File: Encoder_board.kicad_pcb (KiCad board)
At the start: 2 copper layers, 71 parts, among them J1 Conn_01x05_Socket_RS485, J2 CAN_OUT, J3 Conn_01x05_Socket_Encoder4, J4 Conn_01x05_Socket_Encoder1, J5 Conn_01x05_Socket_Encoder2, J6 Conn_01x05_Socket_Encoder5, J7 ST-Link_pinsocket, J8 Conn_01x05_Socket_Encoder3, SW1 SW_Boot, SW2 SW_Reset, SW3 SW_DIP_x02_CANnum, SW4 SW_User, U1 XT60_M, U2 UTRS485G-S08-R, U3 UTRS485G-S08-R, U4 MCP2562-E-P, U5 BA05CC0FP, U6 BA033CC0FP, U7 STM32G431KBTx

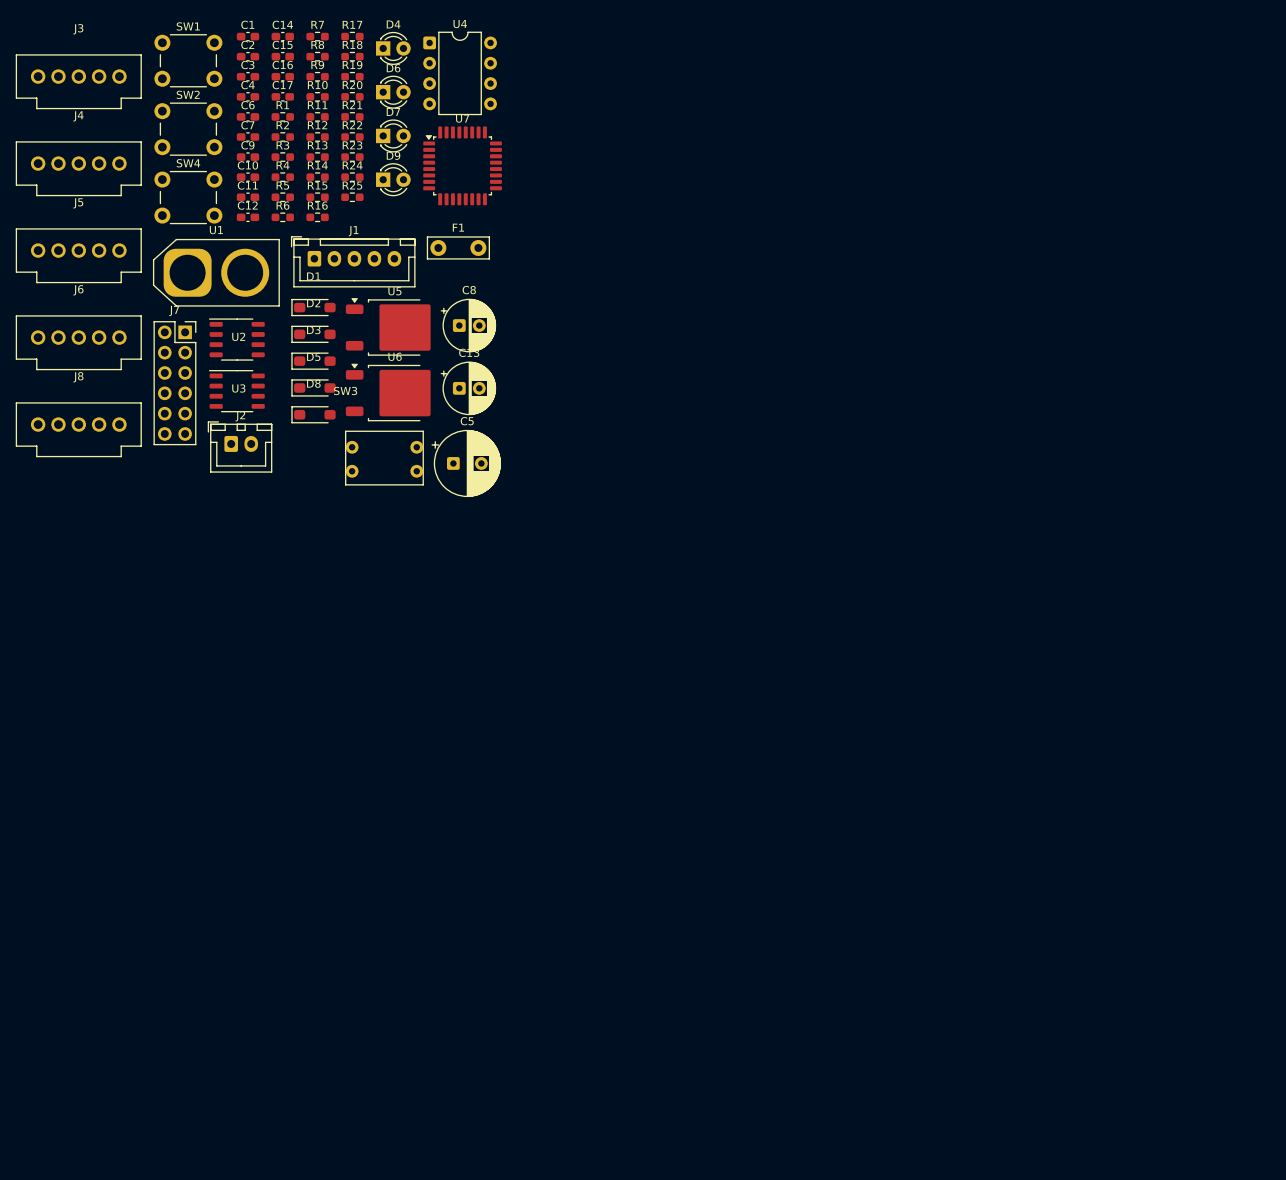
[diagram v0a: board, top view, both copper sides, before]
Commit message: 部品を配置
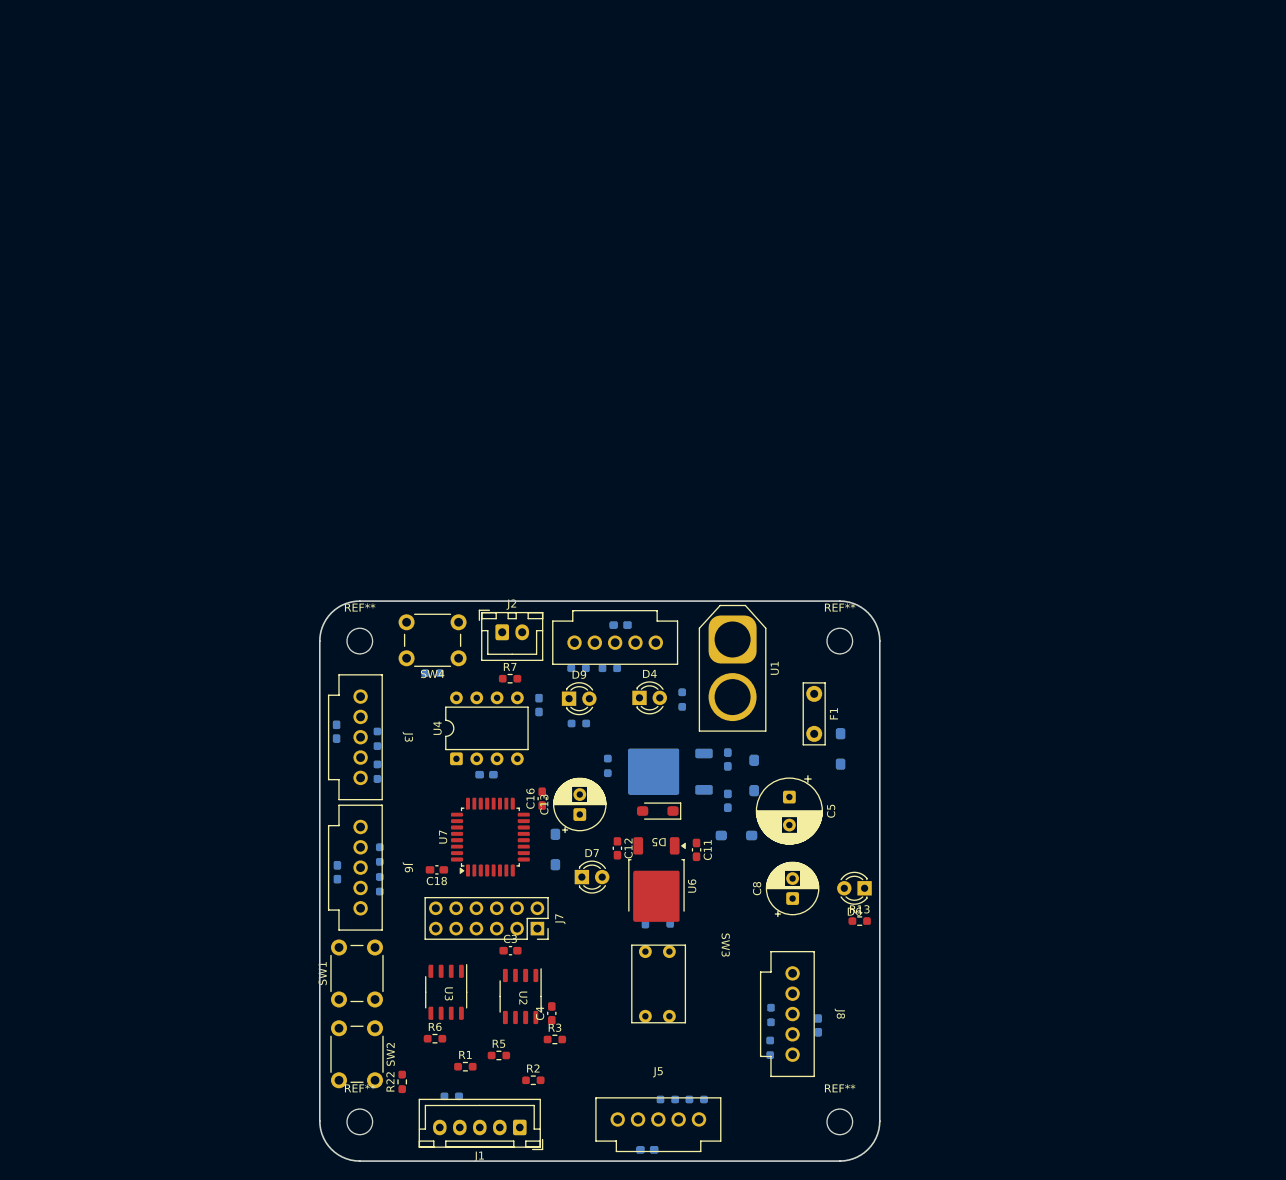
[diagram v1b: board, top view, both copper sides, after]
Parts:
- added C18: 0.1u, Capacitor_SMD:C_0603_1608Metric_Pad1.08x0.95mm_HandSolder, F.Cu at (74.7, 133.6)
- added REF**: MountingHole_3.2mm_M3, MountingHole:MountingHole_3.2mm_M3, F.Cu at (125.1, 105.0)
- added REF**: MountingHole_3.2mm_M3, MountingHole:MountingHole_3.2mm_M3, F.Cu at (65.1, 165.1)
- added REF**: MountingHole_3.2mm_M3, MountingHole:MountingHole_3.2mm_M3, F.Cu at (65.1, 105.0)
- added REF**: MountingHole_3.2mm_M3, MountingHole:MountingHole_3.2mm_M3, F.Cu at (125.1, 165.1)
- C1, C10, C14, C15, C17, C2, C6, C7, C9, D1, D2, D3, D8, R10, R11, R12, R14, R15, R16, R17, R18, R19, R20, R21, R23, R24, R25, R4, R8, R9, U5: moved to B.Cu
- moved C14 146.4 mm to (101.0, 168.6), turned to 180 degrees
- moved R17 139.7 mm to (107.2, 162.3)
- moved C17 134.0 mm to (122.4, 153.0), turned to 90 degrees
- moved J5 130.6 mm to (102.5, 159.3)
- moved R21 127.5 mm to (116.4, 155.8), turned to -90 degrees
- moved R20 126.1 mm to (116.5, 151.7), turned to 90 degrees
- moved J8 123.5 mm to (124.7, 151.7), turned to -90 degrees
- moved R2 122.0 mm to (86.8, 159.9)
- moved SW1 121.6 mm to (62.5, 149.8), turned to 90 degrees
- moved R15 121.0 mm to (103.6, 162.3), turned to 180 degrees
- moved R1 120.9 mm to (78.3, 158.2)
- moved C4 120.7 mm to (89.1, 151.5), turned to 90 degrees
- moved R22 118.3 mm to (70.4, 160.1), turned to 90 degrees
- moved SW2 117.7 mm to (67.0, 153.4), turned to -90 degrees
- moved R13 117.1 mm to (127.6, 140.0)
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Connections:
- R22 pad 1: +3V3 -> +5V
- U7 pad 10: User_LED -> CAN_num2
- U7 pad 13: CAN_num2 -> User_LED
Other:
- board outline added: 70 x 70 mm

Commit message: 配線終了。あとはシルク
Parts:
- R22: moved to B.Cu
- R4: moved to F.Cu
- SW3: footprint mylib:DIP_sw_02_9.7_6.7 -> Button_Switch_THT:SW_DIP_SPSTx02_Slide_6.7x6.64mm_W7.62mm_P2.54mm_LowProfile
- moved R22 84.4 mm to (142.2, 115.7), turned to 180 degrees
- moved SW2 81.7 mm to (141.4, 119.7), turned to 0 degrees
- moved R24 77.7 mm to (171.0, 106.2), turned to 180 degrees
- moved C14 76.7 mm to (149.2, 108.9), turned to -90 degrees
- moved R23 76.1 mm to (171.0, 103.5), turned to 180 degrees
- moved R16 75.0 mm to (116.7, 75.0)
- moved J6 74.5 mm to (119.4, 76.9)
- moved C15 74.1 mm to (111.3, 78.3)
- moved R18 73.7 mm to (116.6, 80.3)
- moved SW1 73.5 mm to (111.2, 94.7)
- moved SW3 73.4 mm to (167.8, 103.6), turned to 0 degrees
- moved R25 73.3 mm to (135.1, 68.2), turned to 90 degrees
- moved SW4 72.7 mm to (135.9, 63.9)
- moved R1 72.4 mm to (134.5, 112.6)
- moved U3 71.7 mm to (134.3, 107.7)
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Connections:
- R22 pad 1: +5V -> +3V3
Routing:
- net GND: track 0.00 -> 406.2 mm, vias 0 -> 13
- net +5V: track 0.00 -> 264.2 mm, vias 0 -> 8
- net +3V3: track 0.00 -> 161.0 mm, vias 0 -> 9
- net RESET: track 0.00 -> 46.0 mm
- net CAN_num1: track 0.00 -> 43.3 mm, vias 0 -> 2
- net CAN_num2: track 0.00 -> 43.3 mm, vias 0 -> 2
- net En3_B: track 0.00 -> 40.4 mm
- net En3_A: track 0.00 -> 37.2 mm
- net User_button: track 0.00 -> 34.5 mm, vias 0 -> 3
- net En4_B: track 0.00 -> 31.5 mm, vias 0 -> 1
- net En5_B: track 0.00 -> 31.5 mm
- net En1_A: track 0.00 -> 29.1 mm
- net En2_A: track 0.00 -> 27.8 mm, vias 0 -> 1
- net En4_A: track 0.00 -> 27.5 mm, vias 0 -> 1
- net En1_B: track 0.00 -> 27.1 mm
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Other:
- outline, holes or cut-outs redrawn

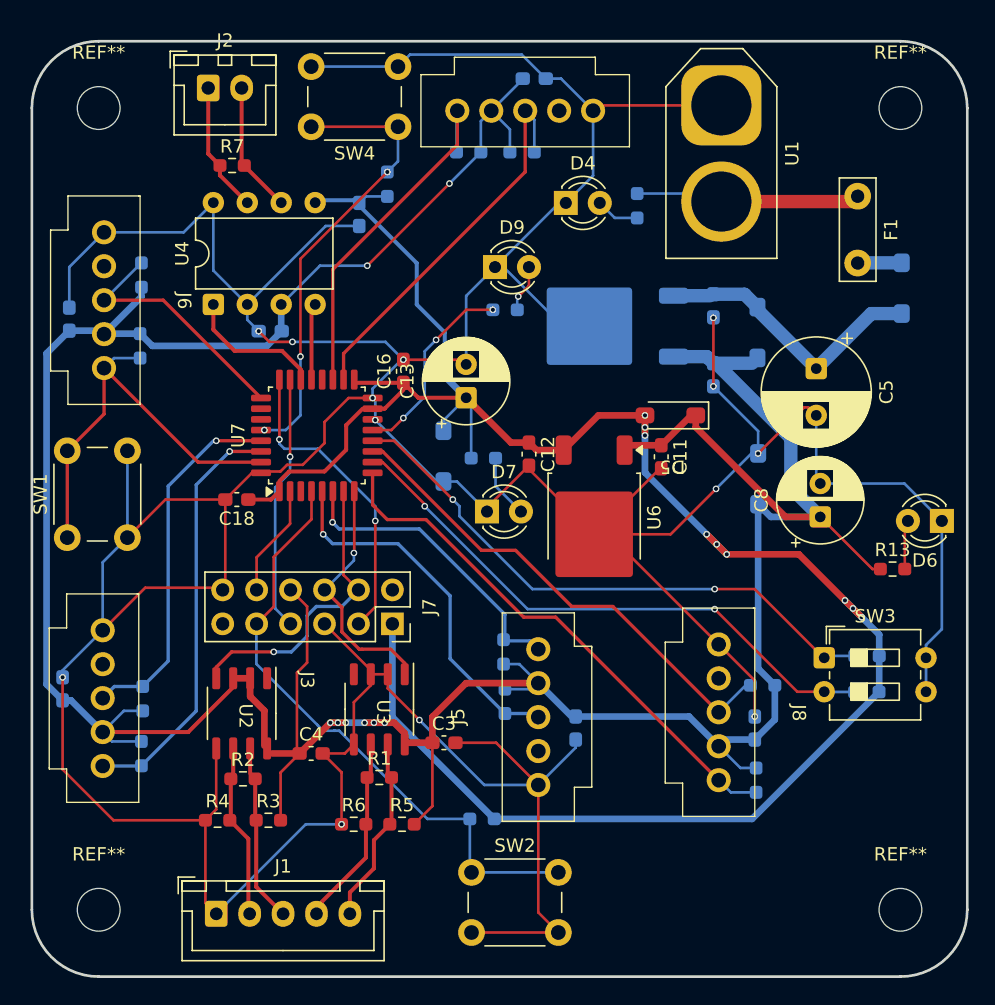
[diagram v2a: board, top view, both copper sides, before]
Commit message: 塗りつぶしとビアうち終了
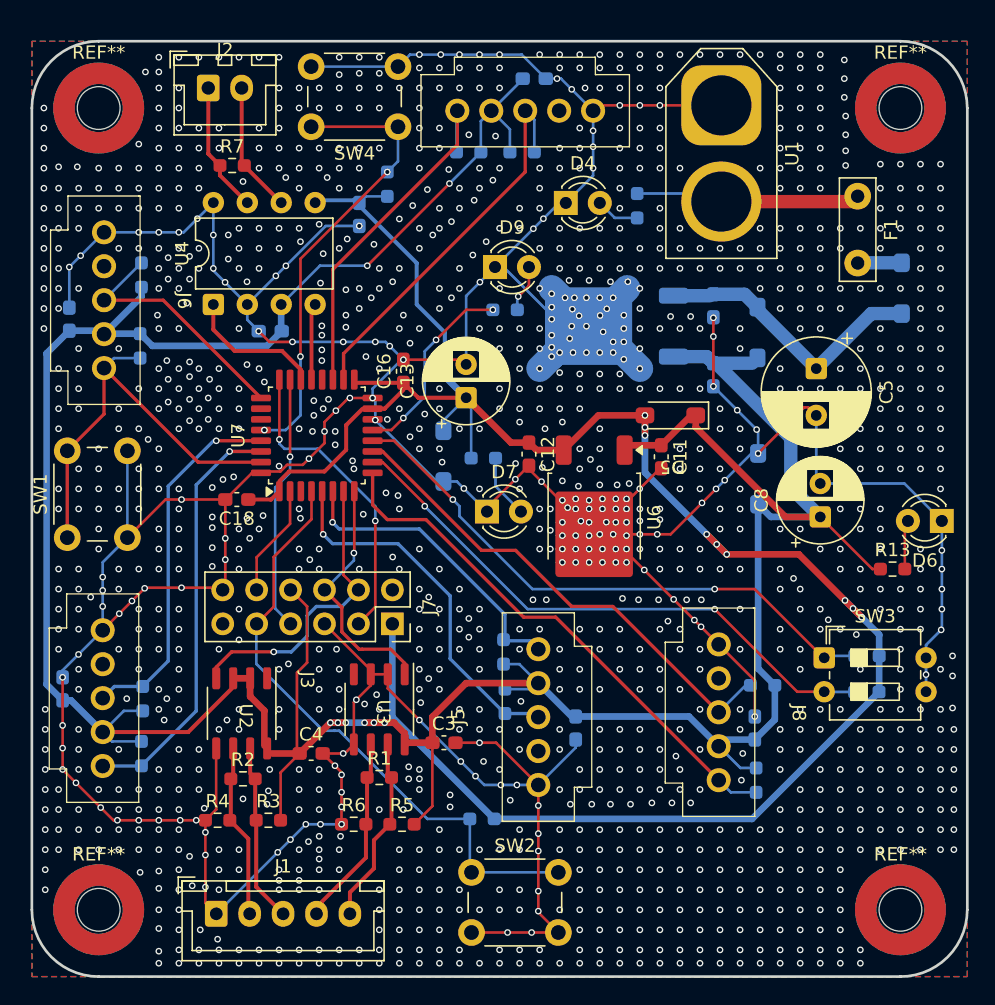
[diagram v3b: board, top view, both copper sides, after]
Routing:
- net GND: track 406.2 -> 477.2 mm, vias 13 -> 1386
- added copper zone on B.Cu, net GND
- added copper zone on F.Cu, net GND

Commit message: とりあえず完成
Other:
- board text added: "1"
- board text added: "12V"
- board text added: "12V_IN"
- board text added: "2"
- board text added: "3V3"
- board text added: "5V"
- board text added: "A"
- board text added: "B"
- board text added: "Boot"
- board text added: "CAN"
- board text added: "CAN_num"
- board text added: "En_1"
- board text added: "En_2"
- board text added: "En_3"
- board text added: "En_4"
- board text added: "En_5"
- board text added: "GND"
- board text added: "H"
- board text added: "L"
- board text added: "RS485"
- board text added: "RX"
- board text added: "Reset"
- board text added: "ST_Link"
- board text added: "TX"
- board text added: "User"
- board text added: "User_LED"
- board text added: "X"

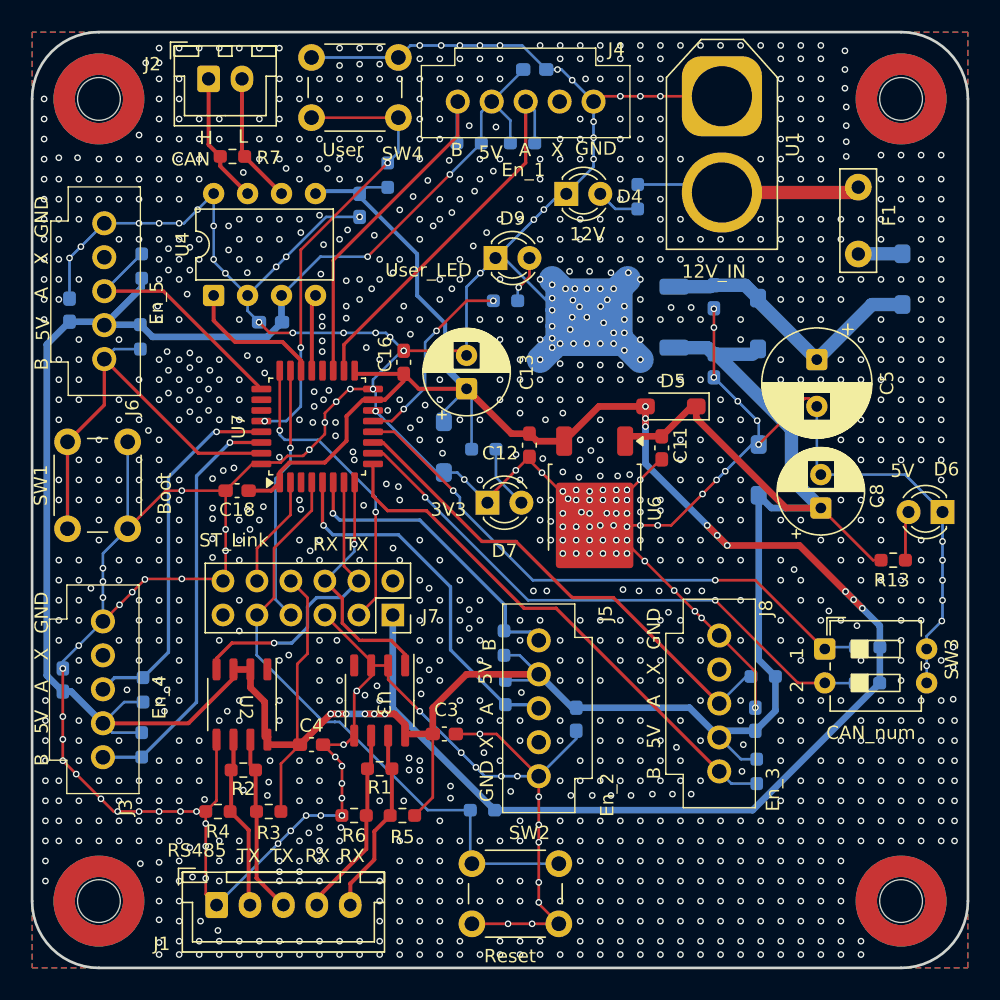
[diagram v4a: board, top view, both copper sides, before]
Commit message: ねじ穴の位置を修正
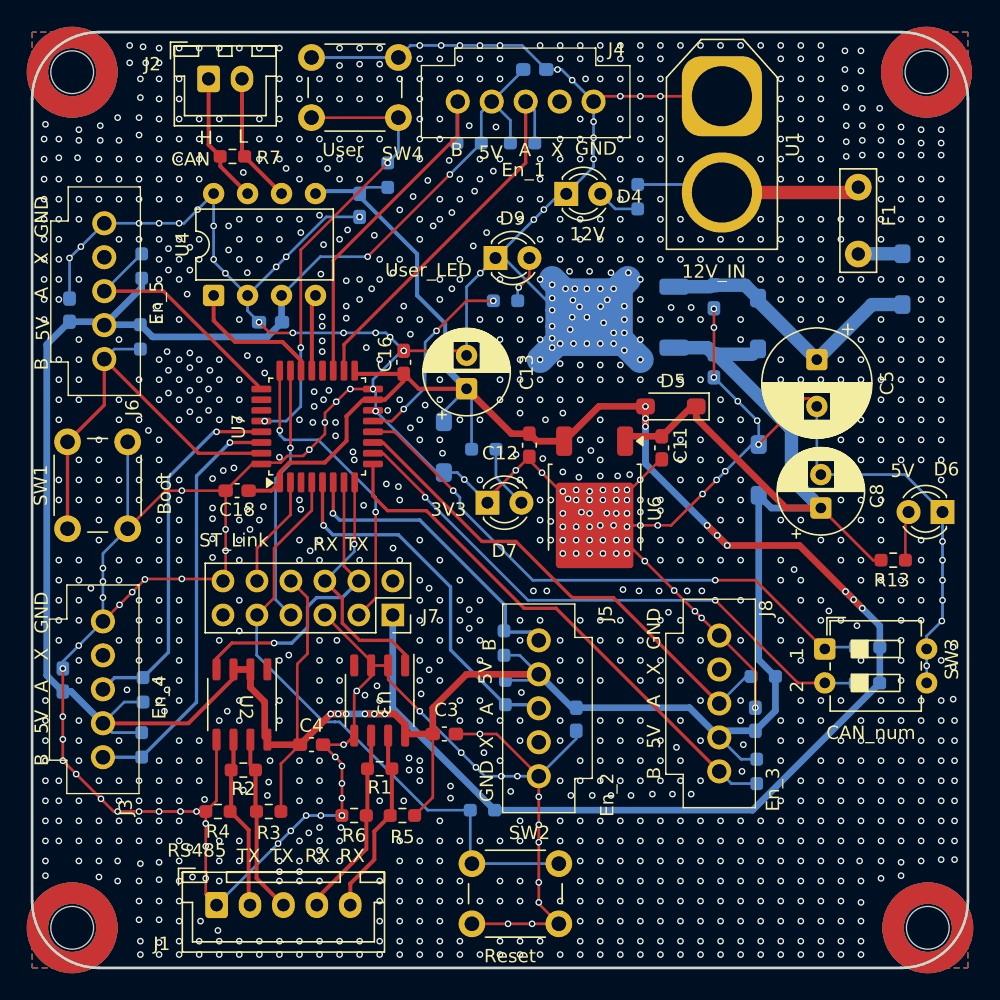
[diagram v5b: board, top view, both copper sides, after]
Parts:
- moved REF** 2.83 mm to (111.5, 124.5)
- moved REF** 2.83 mm to (111.5, 60.5)
- moved REF** 2.83 mm to (175.5, 124.5)
- moved REF** 2.76 mm to (175.4, 60.5)
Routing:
- net GND: vias 1386 -> 1435

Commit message: 基板名を追加
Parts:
- added REF**: rogiken, mylib:rogiken, F.Cu at (167.0, 120.4)
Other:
- board text added: "NHK2026_EncoderBoard"
